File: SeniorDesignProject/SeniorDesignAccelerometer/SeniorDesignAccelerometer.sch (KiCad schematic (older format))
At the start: 2 parts, among them J1 CONN_02X05, J2 RJ45

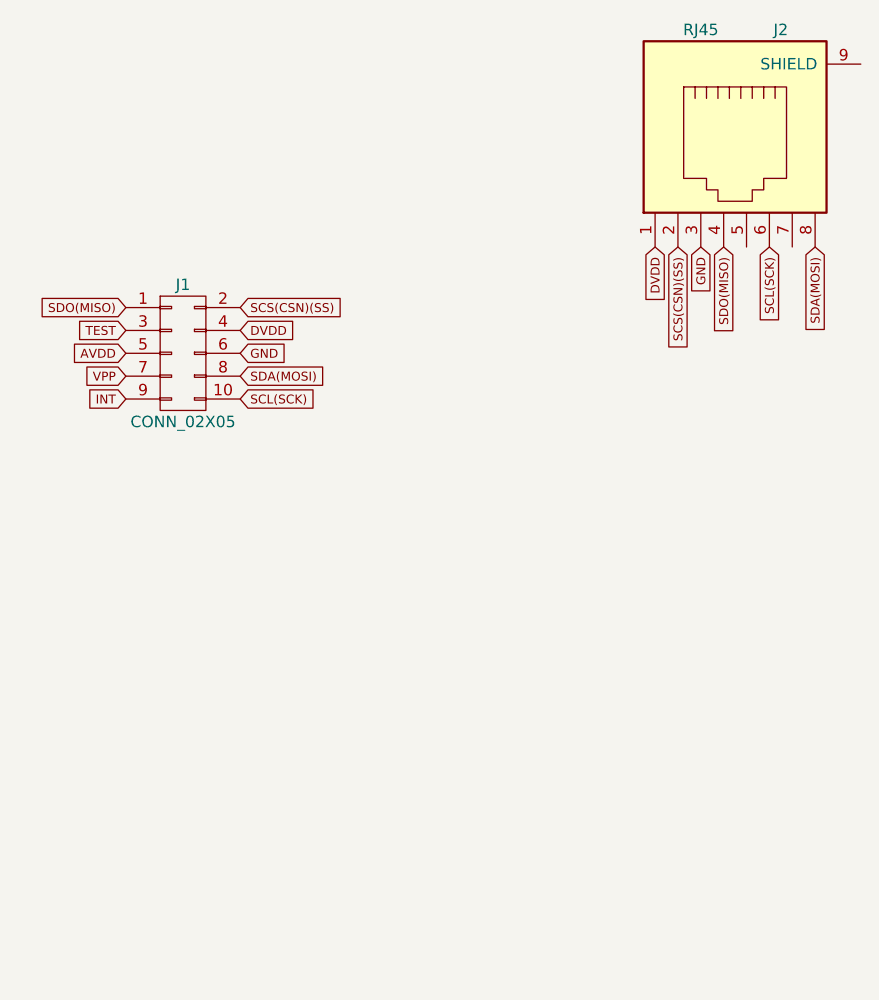
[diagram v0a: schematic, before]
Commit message: Updates to accelerometer board and main board
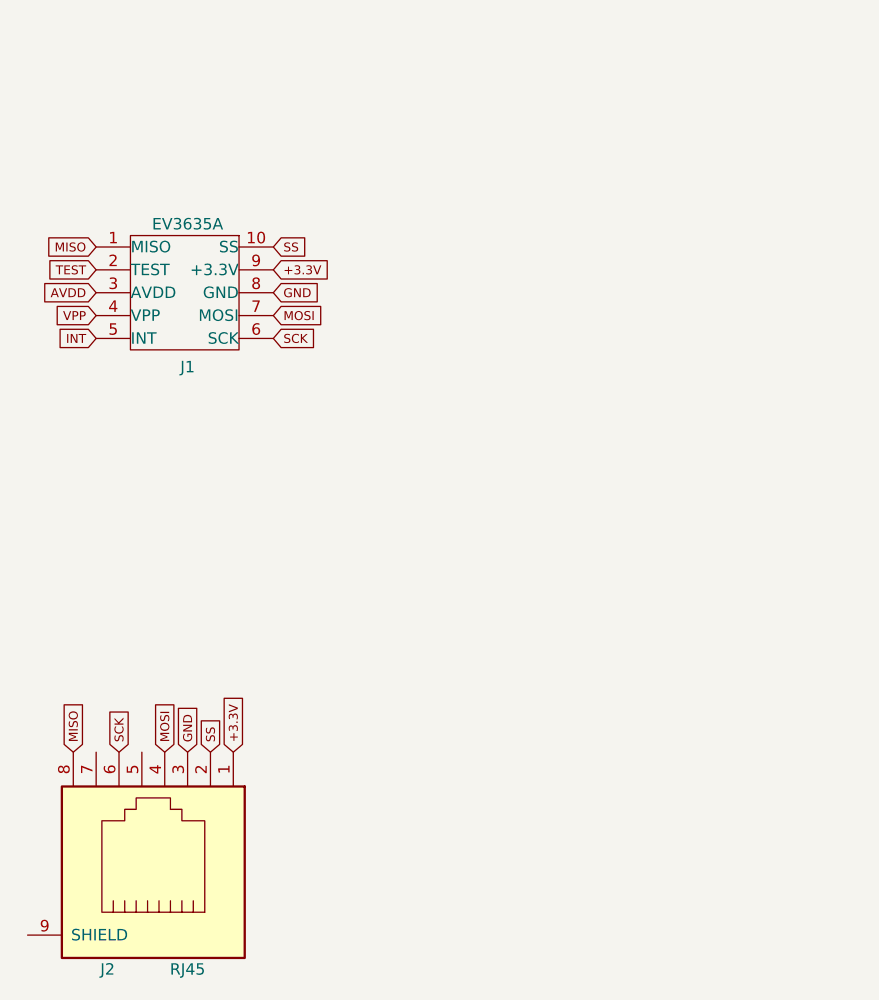
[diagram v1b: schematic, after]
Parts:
- removed J1: CONN_02X05, SeniorDesignFootprints:EV3635A, symbol CONN_02X05
- added J1: EV3635A, SeniorDesignFootprints:EV3635A, symbol EV3635A
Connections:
- net AVDD: now also J1.3 (AVDD)
- net GND: now also J1.8 (GND)
- net INT: now also J1.5 (INT)
- net TEST: now also J1.2 (TEST)
- net VPP: now also J1.4 (VPP)
- net DVDD renamed +3.3V
- net +3.3V: now also J1.9 (+3.3V)
- net SCL(SCK) renamed SCK
- net SCK: now also J1.6 (SCK)
- net SCS(CSN)(SS) renamed SS
- net SS: now also J1.10 (SS)
- net SDA(MOSI) renamed MISO
- net MISO: now also J1.1 (MISO)
- net SDO(MISO) renamed MOSI
- net MOSI: now also J1.7 (MOSI)
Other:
- moved on the sheet: J2
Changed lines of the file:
@@
 LIBS:contrib
 LIBS:valves
+LIBS:SeniorDesignSchematics
+LIBS:SeniorDesignAccelerometer-cache
 EELAYER 25 0
 EELAYER END
@@
 Comment4 ""
 $EndDescr
-$Comp
-L CONN_02X05 J1
-U 1 1 58C45E17
-P 5940 3645
-F 0 "J1" H 5940 3945 50  0000 C CNN
-F 1 "CONN_02X05" H 5940 3345 50  0000 C CNN
-F 2 "SeniorDesignFootprints:EV3635A" H 5940 2445 50  0001 C CNN
-F 3 "" H 5940 2445 50  0001 C CNN
-	1    5940 3645
-	1    0    0    -1
-$EndComp
-Text GLabel 5690 3445 0    39   Input ~ 0
-SDO(MISO)
-Text GLabel 5690 3545 0    39   Input ~ 0
+Text GLabel 5560 3180 0    39   Input ~ 0
+MISO
+Text GLabel 5560 3280 0    39   Input ~ 0
 TEST
-Text GLabel 5690 3645 0    39   Input ~ 0
+Text GLabel 5560 3380 0    39   Input ~ 0
 AVDD
-Text GLabel 5690 3745 0    39   Input ~ 0
+Text GLabel 5560 3480 0    39   Input ~ 0
 VPP
-Text GLabel 5690 3845 0    39   Input ~ 0
+Text GLabel 5560 3580 0    39   Input ~ 0
 INT
-Text GLabel 6190 3845 2    39   Input ~ 0
-SCL(SCK)
-Text GLabel 6190 3745 2    39   Input ~ 0
-SDA(MOSI)
-Text GLabel 6190 3645 2    39   Input ~ 0
+Text GLabel 6335 3580 2    39   Input ~ 0
+SCK
+Text GLabel 6335 3480 2    39   Input ~ 0
+MOSI
+Text GLabel 6335 3380 2    39   Input ~ 0
 GND
-Text GLabel 6190 3545 2    39   Input ~ 0
-DVDD
-Text GLabel 6190 3445 2    39   Input ~ 0
-SCS(CSN)(SS)
+Text GLabel 6335 3280 2    39   Input ~ 0
++3.3V
+Text GLabel 6335 3180 2    39   Input ~ 0
+SS
 $Comp
 L RJ45 J2
 U 1 1 58C46065
-P 8355 2730
-F 0 "J2" H 8555 3230 50  0000 C CNN
-F 1 "RJ45" H 8205 3230 50  0000 C CNN
-F 2 "Connect:RJ45_8" H 8355 2730 50  0001 C CNN
-F 3 "" H 8355 2730 50  0001 C CNN
-	1    8355 2730
+P 5810 5840
+F 0 "J2" H 6010 6340 50  0000 C CNN
+F 1 "RJ45" H 5660 6340 50  0000 C CNN
+F 2 "Connect:RJ45_8" H 5810 5840 50  0001 C CNN
+F 3 "" H 5810 5840 50  0001 C CNN
+	1    5810 5840
+	-1   0    0    1
+$EndComp
+Text GLabel 6160 5390 1    39   Input ~ 0
++3.3V
+Text GLabel 5960 5390 1    39   Input ~ 0
+GND
+Text GLabel 5660 5390 1    39   Input ~ 0
+SCK
+Text GLabel 5460 5390 1    39   Input ~ 0
+MISO
+Text GLabel 5860 5390 1    39   Input ~ 0
+MOSI
+Text GLabel 6060 5390 1    39   Input ~ 0
+SS
+$Comp
+L EV3635A J1
+U 1 1 58CC7116
+P 5960 3380
+F 0 "J1" H 5960 3055 50  0000 C CNN
+F 1 "EV3635A" H 5960 3680 50  0000 C CNN
+F 2 "SeniorDesignFootprints:EV3635A" H 5960 2180 50  0001 C CNN
+F 3 "" H 5960 2180 50  0001 C CNN
+	1    5960 3380
 	1    0    0    -1
 $EndComp
-Text GLabel 8005 3180 3    39   Input ~ 0
-DVDD
-Text GLabel 8205 3180 3    39   Input ~ 0
-GND
-Text GLabel 8505 3180 3    39   Input ~ 0
-SCL(SCK)
-Text GLabel 8705 3180 3    39   Input ~ 0
-SDA(MOSI)
-Text GLabel 8305 3180 3    39   Input ~ 0
-SDO(MISO)
-Text GLabel 8105 3180 3    39   Input ~ 0
-SCS(CSN)(SS)
 $EndSCHEMATC
